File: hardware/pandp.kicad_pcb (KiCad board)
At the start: 2 copper layers, 116 x 55.5 mm, 93 parts, among them IC1 ADP2303-5, IC2 DRV8830, P1 CONN_01X02, P10 CONN_01X04, P11 CONN_01X02, P12 CONN_02X04, P13 CONN_01X02, P14 CONN_01X04, P15 CONN_01X04, P16 CONN_01X03, P17 CONN_01X03, P18 CONN_01X03, P19 CONN_01X03, P2 CONN_01X03, P20 CONN_01X03, P21 CONN_01X03, P22 CONN_02X03, P23 CONN_02X03, P24 CONN_02X03, P25 CONN_02X03, P26 CONN_01X03, P27 CONN_01X03, P28 CONN_01X03, P29 CONN_01X03, P3 CONN_01X02, P30 CONN_01X04, P31 CONN_01X04, P32 CONN_01X04, P33 CONN_01X04, P4 CONN_01X03, P5 CONN_01X02, P6 CONN_01X03, P7 CONN_01X03, P8 USB_OTG, P9 CONN_01X02, Q1 IRF540N, Q2 IRF540N, SW1 SW_PUSH, U1 AP1117D33, U2 STM32F103RC, Y1 Crystal_Small - 2101357 on el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, Y2 Crystal_Small - 2063972 on el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

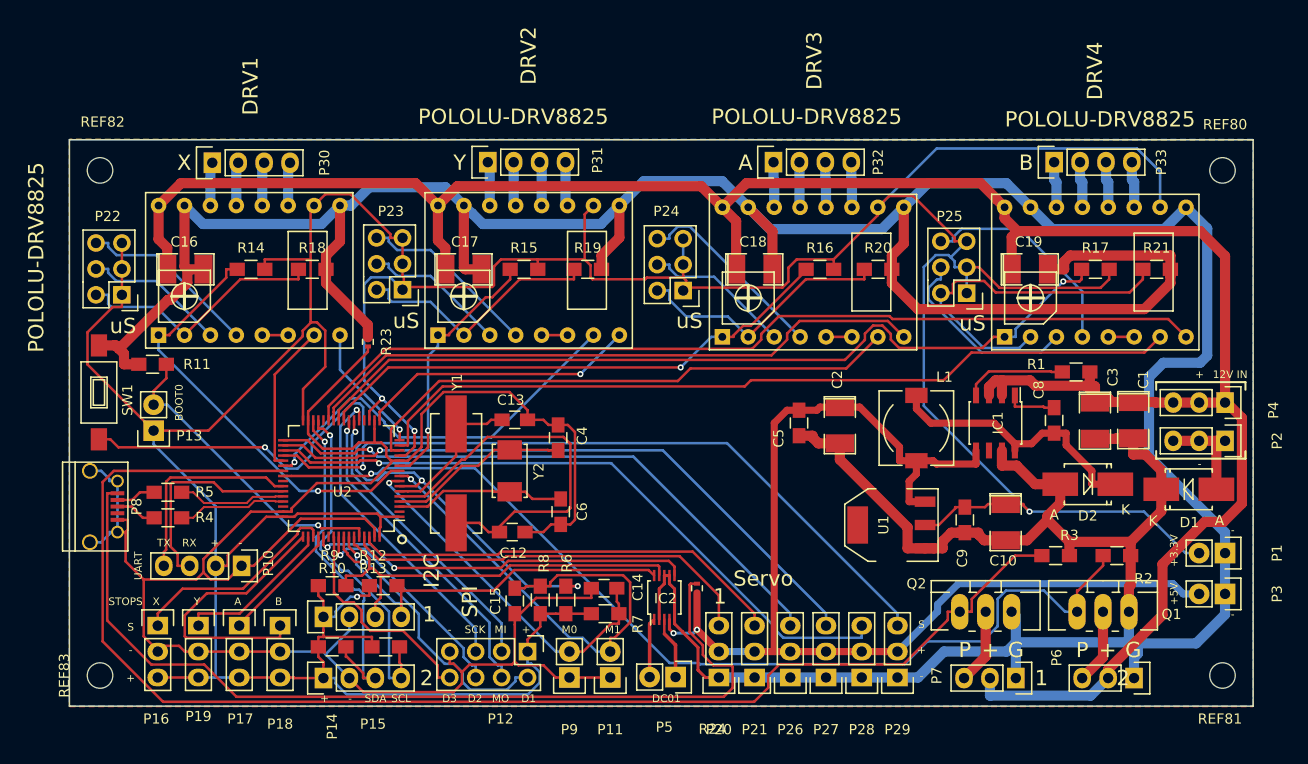
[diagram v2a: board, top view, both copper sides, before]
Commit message: added pullup for usb
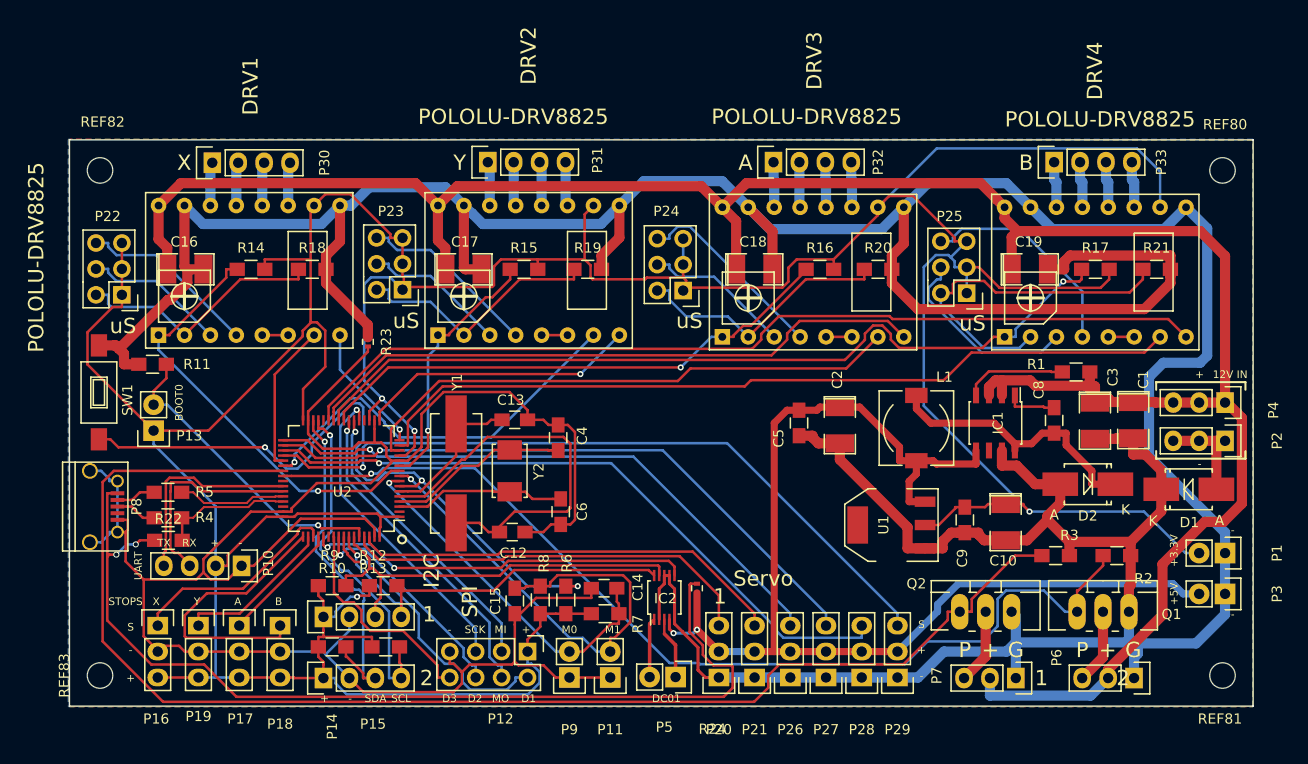
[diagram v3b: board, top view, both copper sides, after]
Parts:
- added R22: 4.7k, Resistors_SMD:R_0805_HandSoldering, F.Cu at (92.2, 101.0)
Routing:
- net +5VL: track 91.9 -> 97.2 mm, vias 0 -> 2
- net USB_D_P: track 10.6 -> 12.9 mm
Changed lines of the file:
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@@
 (kicad_pcb (version 4) (host pcbnew 4.0.2+dfsg1-stable)
   (general
-    (links 267)
+    (links 269)
     (no_connects 0)
     (area 82.424999 61.674999 198.575001 117.325001)
     (thickness 1.6)
     (drawings 79)
-    (tracks 1240)
+    (tracks 1254)
     (zones 0)
-    (modules 93)
+    (modules 94)
     (nets 96)
   )
@@
       (net 90 GNDD))
   )
+  (module Resistors_SMD:R_0805_HandSoldering (layer F.Cu)
+    (at 92.2 101)
+    (descr "Resistor SMD 0805, hand soldering")
+    (tags "resistor 0805")
+    (attr smd)
+    (fp_text reference R22 (at 0 -2.1) (layer F.SilkS)
+      (effects (font (size 1 1) (thickness 0.15)))
+    )
+    (fp_text value 4.7k (at 0 2.1) (layer F.Fab)
+      (effects (font (size 1 1) (thickness 0.15)))
+    )
+    (fp_line (start -2.4 -1) (end 2.4 -1) (layer F.CrtYd) (width 0.05))
+    (fp_line (start -2.4 1) (end 2.4 1) (layer F.CrtYd) (width 0.05))
+    (fp_line (start -2.4 -1) (end -2.4 1) (layer F.CrtYd) (width 0.05))
+    (fp_line (start 2.4 -1) (end 2.4 1) (layer F.CrtYd) (width 0.05))
+    (fp_line (start 0.6 0.875) (end -0.6 0.875) (layer F.SilkS) (width 0.15))
+    (fp_line (start -0.6 -0.875) (end 0.6 -0.875) (layer F.SilkS) (width 0.15))
+    (pad 1 smd rect (at -1.35 0) (size 1.5 1.3) (layers F.Cu F.Paste F.Mask)
+      (net 92 +5VL))
+    (pad 2 smd rect (at 1.35 0) (size 1.5 1.3) (layers F.Cu F.Paste F.Mask)
+      (net 88 USB_D_P))
+    (model Resistors_SMD.3dshapes/R_0805_HandSoldering.wrl
+      (at (xyz 0 0 0))
+      (scale (xyz 1 1 1))
+      (rotate (xyz 0 0 0))
+    )
+  )
   (gr_circle (center 115.1 100.9) (end 115.1 101.3) (layer F.SilkS) (width 0.2))
   (gr_text DC01 (at 141 116.5) (layer F.SilkS)
@@
   (segment (start 88.1322 97.6921) (end 88.1401 97.7) (width 0.25) (layer F.Cu) (net 61))
   (segment (start 87.2072 97.6921) (end 88.1322 97.6921) (width 0.25) (layer F.Cu) (net 61))
-  (segment (start 94.29 103.5) (end 93.1011 103.5) (width 0.25) (layer F.Cu) (net 62))
-  (segment (start 97.5168 96.1927) (end 103.445 96.1927) (width 0.25) (layer F.Cu) (net 62))
-  (segment (start 96.6334 95.3093) (end 97.5168 96.1927) (width 0.25) (layer F.Cu) (net 62))
-  (segment (start 92.6157 95.3093) (end 96.6334 95.3093) (width 0.25) (layer F.Cu) (net 62))
-  (segment (start 92.4293 95.4957) (end 92.6157 95.3093) (width 0.25) (layer F.Cu) (net 62))
-  (segment (start 92.4293 101.6393) (end 92.4293 95.4957) (width 0.25) (layer F.Cu) (net 62))
-  (segment (start 93.1011 102.3111) (end 92.4293 101.6393) (width 0.25) (layer F.Cu) (net 62))
-  (segment (start 93.1011 103.5) (end 93.1011 102.3111) (width 0.25) (layer F.Cu) (net 62))
-  (segment (start 91.9789 101.9298) (end 91.75 102.1587) (width 0.25) (layer F.Cu) (net 63))
-  (segment (start 91.9789 95.2539) (end 91.9789 101.9298) (width 0.25) (layer F.Cu) (net 63))
-  (segment (start 92.3889 94.8439) (end 91.9789 95.2539) (width 0.25) (layer F.Cu) (net 63))
-  (segment (start 101.7709 94.8439) (end 92.3889 94.8439) (width 0.25) (layer F.Cu) (net 63))
-  (segment (start 102.6197 95.6927) (end 101.7709 94.8439) (width 0.25) (layer F.Cu) (net 63))
-  (segment (start 103.445 95.6927) (end 102.6197 95.6927) (width 0.25) (layer F.Cu) (net 63))
-  (segment (start 91.75 103.5) (end 91.75 102.1587) (width 0.25) (layer F.Cu) (net 63))
+  (segment (start 94.517699 95.317699) (end 95.3927 96.1927) (width 0.25) (layer F.Cu) (net 62))
+  (segment (start 95.3927 96.1927) (end 103.445 96.1927) (width 0.25) (layer F.Cu) (net 62))
+  (segment (start 92.429699 95.382699) (end 92.494699 95.317699) (width 0.25) (layer F.Cu) (net 62))
+  (segment (start 92.4 96.2) (end 92.429699 96.170301) (width 0.25) (layer F.Cu) (net 62))
+  (segment (start 92.429699 96.170301) (end 92.429699 95.382699) (width 0.25) (layer F.Cu) (net 62))
+  (segment (start 92.494699 95.317699) (end 94.517699 95.317699) (width 0.25) (layer F.Cu) (net 62))
+  (segment (start 92.4 101.835002) (end 92.4 96.2) (width 0.25) (layer F.Cu) (net 62))
+  (segment (start 93.1764 102.234) (end 92.798998 102.234) (width 0.25) (layer F.Cu) (net 62))
+  (segment (start 94.29 103.3476) (end 93.1764 102.234) (width 0.25) (layer F.Cu) (net 62))
+  (segment (start 94.29 103.5) (end 94.29 103.3476) (width 0.25) (layer F.Cu) (net 62))
+  (segment (start 92.798998 102.234) (end 92.4 101.835002) (width 0.25) (layer F.Cu) (net 62))
+  (segment (start 91.75 102.234) (end 91.75 103.5) (width 0.25) (layer F.Cu) (net 63))
+  (segment (start 91.949989 95.225998) (end 91.949989 102.034011) (width 0.25) (layer F.Cu) (net 63))
+  (segment (start 94.704099 94.867688) (end 92.308299 94.867688) (width 0.25) (layer F.Cu) (net 63))
+  (segment (start 95.52911 95.6927) (end 94.704099 94.867688) (width 0.25) (layer F.Cu) (net 63))
+  (segment (start 92.308299 94.867688) (end 91.949989 95.225998) (width 0.25) (layer F.Cu) (net 63))
+  (segment (start 103.445 95.6927) (end 95.52911 95.6927) (width 0.25) (layer F.Cu) (net 63))
+  (segment (start 91.949989 102.034011) (end 91.75 102.234) (width 0.25) (layer F.Cu) (net 63))
   (via (at 111.2638 103.1229) (size 0.6) (layers F.Cu B.Cu) (net 64))
   (segment (start 127.395 114.443) (end 126.2061 114.443) (width 0.25) (layer B.Cu) (net 64))
@@
   (segment (start 116.2733 94.3752) (end 113.4386 94.3752) (width 0.25) (layer B.Cu) (net 87))
   (segment (start 117.0357 95.1376) (end 116.2733 94.3752) (width 0.25) (layer B.Cu) (net 87))
+  (segment (start 93.55 101) (end 93.55 98.8383) (width 0.25) (layer F.Cu) (net 88))
+  (segment (start 93.55 98.8383) (end 93.5047 98.793) (width 0.25) (layer F.Cu) (net 88))
   (segment (start 102.695 97.1927) (end 103.445 97.1927) (width 0.2) (layer F.Cu) (net 88))
   (segment (start 102.645 97.1427) (end 102.695 97.1927) (width 0.2) (layer F.Cu) (net 88))
@@
   (segment (start 193.21 91.25) (end 194.9 91.25) (width 1) (layer F.Cu) (net 91))
   (segment (start 194.9 91.25) (end 195.75 91.25) (width 1) (layer F.Cu) (net 91))
+  (segment (start 86.2069 108.8507) (end 86.2069 102.6) (width 0.25) (layer F.Cu) (net 92))
+  (segment (start 86.2069 102.6) (end 86.2069 96.3921) (width 0.25) (layer F.Cu) (net 92))
+  (segment (start 86.4069 102.4) (end 86.2069 102.6) (width 0.25) (layer F.Cu) (net 92))
+  (segment (start 87.1 102.4) (end 86.4069 102.4) (width 0.25) (layer F.Cu) (net 92))
+  (segment (start 89 101.4) (end 88.1 101.4) (width 0.25) (layer B.Cu) (net 92))
+  (segment (start 88.1 101.4) (end 87.1 102.4) (width 0.25) (layer B.Cu) (net 92))
+  (via (at 87.1 102.4) (size 0.6) (drill 0.4) (layers F.Cu B.Cu) (net 92))
+  (segment (start 90.85 101) (end 89.4 101) (width 0.25) (layer F.Cu) (net 92))
+  (segment (start 89.4 101) (end 89 101.4) (width 0.25) (layer F.Cu) (net 92))
+  (via (at 89 101.4) (size 0.6) (drill 0.4) (layers F.Cu B.Cu) (net 92))
   (segment (start 144 105.25) (end 143.3747 105.25) (width 0.25) (layer F.Cu) (net 92))
   (segment (start 87.2072 96.3921) (end 86.2069 96.3921) (width 0.25) (layer F.Cu) (net 92))
-  (segment (start 86.2069 108.8507) (end 86.2069 96.3921) (width 0.25) (layer F.Cu) (net 92))
   (segment (start 90.5292 113.173) (end 86.2069 108.8507) (width 0.25) (layer F.Cu) (net 92))
   (segment (start 95.7089 113.173) (end 90.5292 113.173) (width 0.25) (layer F.Cu) (net 92))
@@
   (segment (start 107.6072 101.6802) (end 107.7981 101.6802) (width 0.25) (layer F.Cu) (net 95))
   (segment (start 107.395 101.468) (end 107.6072 101.6802) (width 0.25) (layer F.Cu) (net 95))
-  (zone (net 1) (net_name GND) (layer B.Cu) (hatch edge 0.508)
+  (zone (net 12) (net_name +12V) (layer F.Cu) (hatch edge 0.508)
     (connect_pads yes (clearance 0.2))
     (min_thickness 0.254)
@@
     (polygon
       (pts
-        (xy 82.5 61.7) (xy 82.5 117.2) (xy 198.5 117.2) (xy 198.5 61.7)
+        (xy 82.5 61.7) (xy 82.5 117.3) (xy 198.5 117.3) (xy 198.5 61.8)
       )
     )
   )
-  (zone (net 12) (net_name +12V) (layer F.Cu) (hatch edge 0.508)
+  (zone (net 1) (net_name GND) (layer B.Cu) (hatch edge 0.508)
     (connect_pads yes (clearance 0.2))
     (min_thickness 0.254)
@@
     (polygon
       (pts
-        (xy 82.5 61.7) (xy 82.5 117.3) (xy 198.5 117.3) (xy 198.5 61.8)
+        (xy 82.4 61.7) (xy 82.4 117.3) (xy 198.5 117.3) (xy 198.5 61.7)
       )
     )
